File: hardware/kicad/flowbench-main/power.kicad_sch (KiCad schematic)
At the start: 38 parts, among them J1 24V IN, J2 PM1 power socket, J3 PM1 signal socket, Q1 SUD50P06-15 (60 V P-ch, DPAK), Q2 MMBT3904, Q3 SUD50P06-15 (60 V P-ch, DPAK), Q4 MMBT3904, Q5 SUD50P06-15 (60 V P-ch, DPAK), Q6 MMBT3904, U1 LM1117-3.3

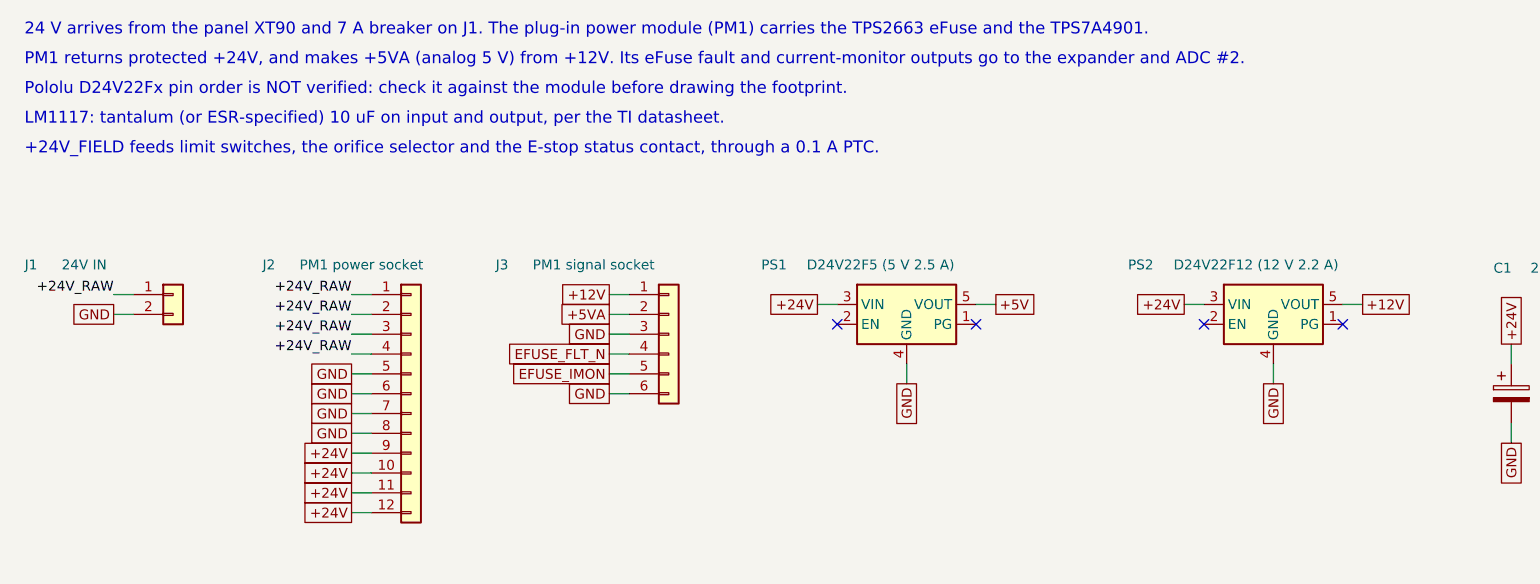
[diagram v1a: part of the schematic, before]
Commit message: KiCad: Pololu D24V22Fx pinout confirmed, corner GND and footprint
Pin order confirmed from Pololu's labelled top view (PG, EN, VIN, GND, VOUT).
Adds the corner GND as pin 6 and a project footprint FlowBench:Pololu_D24V22Fx
(5 pins at 0.1 in plus the corner GND 0.4 in across), with fp-lib-table.

Co-Authored-By: Claude Opus 5.5 <noreply@anthropic.com>
Claude-Session: https://claude.ai/code/session_01QEmmugJA9S77dSDSNcKrPa
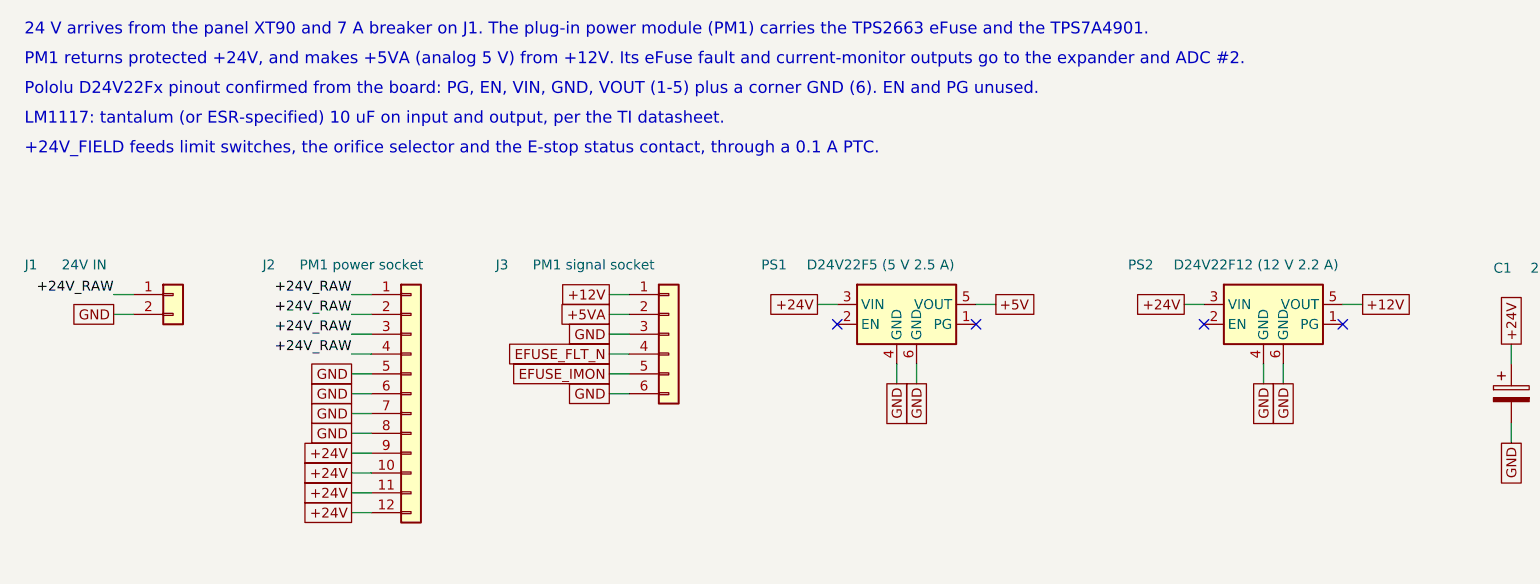
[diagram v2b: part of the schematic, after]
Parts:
- PS1, PS2: footprint Connector_PinSocket_2.54mm:PinSocket_1x05_P2.54mm_Vertical -> FlowBench:Pololu_D24V22Fx
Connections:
- net GND: now also PS1.6 (GND), PS2.6 (GND)
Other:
- note added: "Pololu D24V22Fx pinout confirmed from the board: PG, EN, VIN, GND, VOUT (1-5) plus a corner GND (6). EN and PG unused."
- note removed: "Pololu D24V22Fx pin order is NOT verified: check it against the module before drawing the footprint."

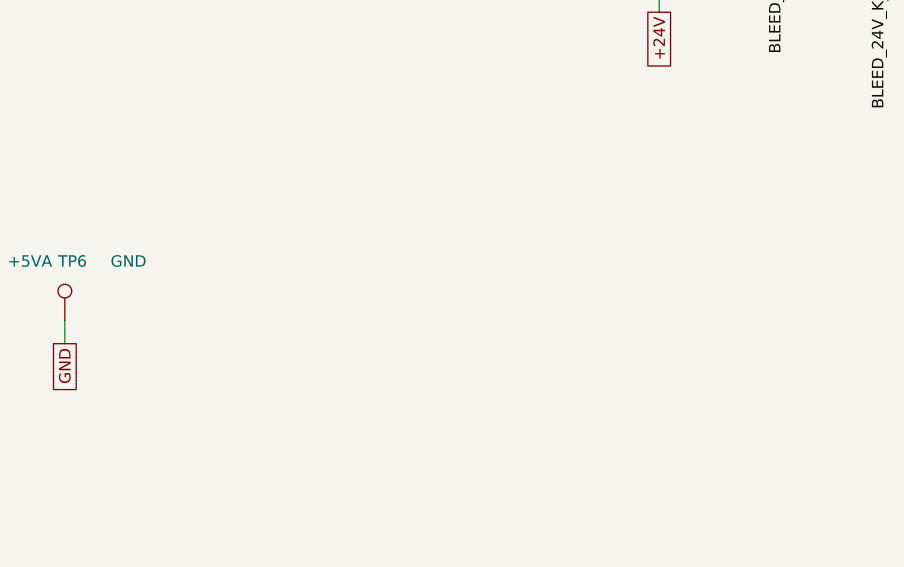
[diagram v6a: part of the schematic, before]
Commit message: KiCad: rev A board placement script and mounting holes
place_rev_a.py (generated by tools/placement.py) sets a 220 x 160 mm outline,
puts the 24 V/actuator connectors on the top edge and sensor connectors on the
bottom edge facing out, the DevKit antenna over the left edge, the RJ45 and
ABP2 ports toward the right edge, ICs at planned spots, and packs every passive
next to the part it serves with 1 mm clearance. Adds four M3 mounting holes
to the schematic. placement-preview.png simulates the result.

Co-Authored-By: Claude Opus 5.5 <noreply@anthropic.com>
Claude-Session: https://claude.ai/code/session_01QEmmugJA9S77dSDSNcKrPa
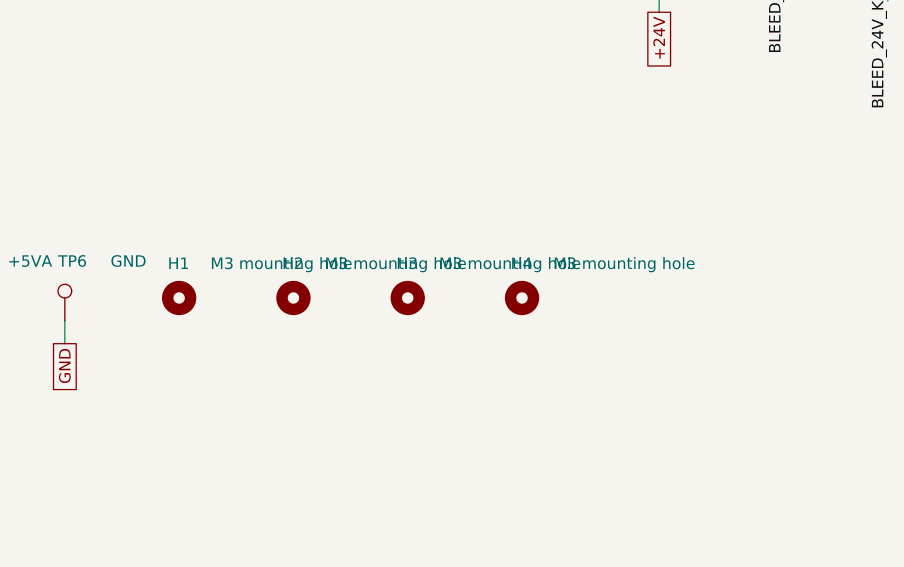
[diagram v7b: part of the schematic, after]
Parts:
- added H1, H2, H3, H4: M3 mounting hole, MountingHole:MountingHole_3.2mm_M3, symbol FlowBench:MountingHole
